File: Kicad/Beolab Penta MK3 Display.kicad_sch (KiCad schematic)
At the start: 6 parts, among them J1 Conn_01x07_Pin

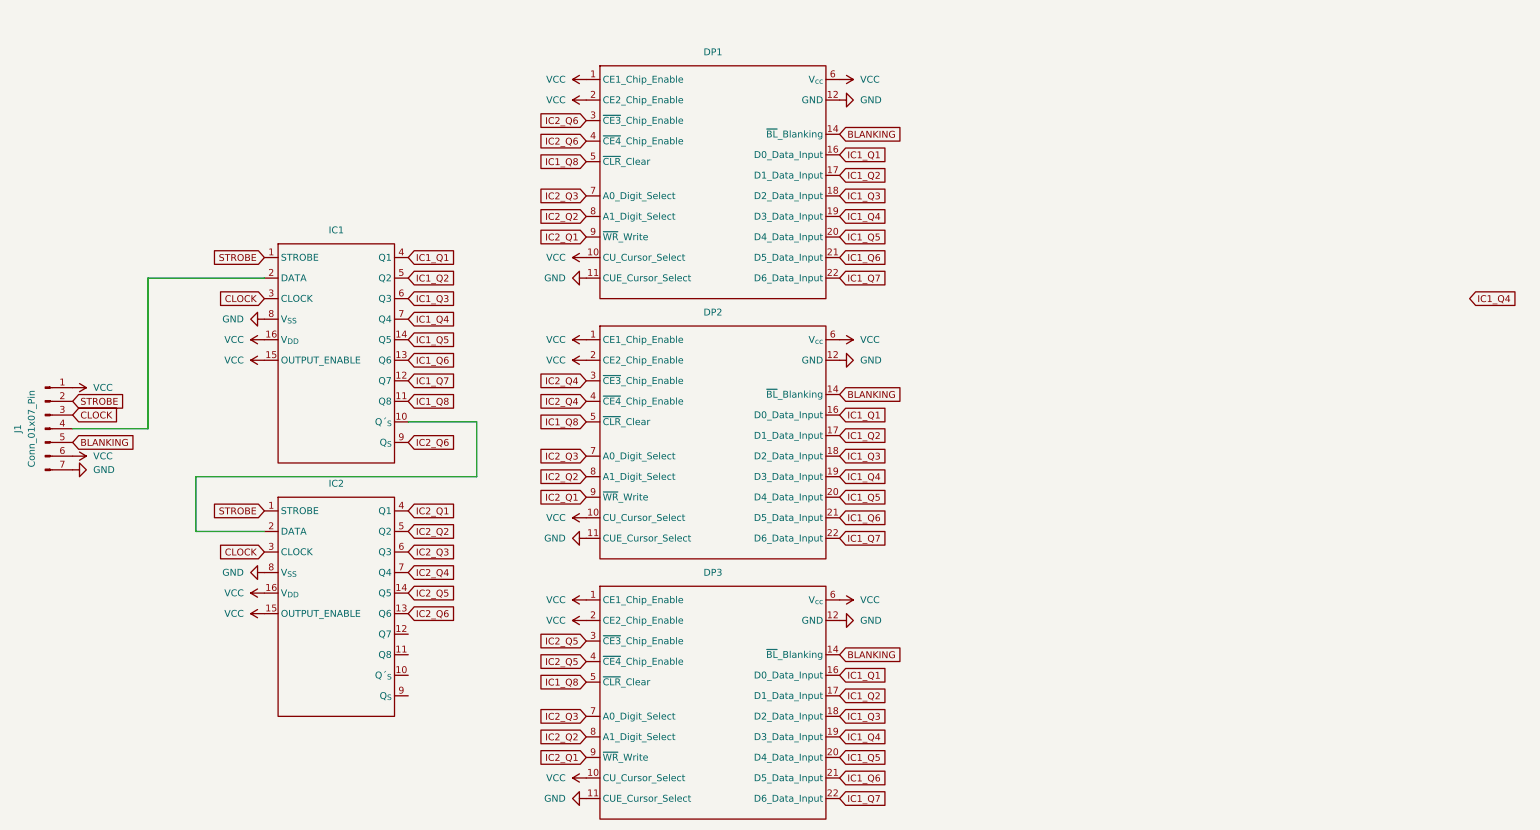
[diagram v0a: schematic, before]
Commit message: Update schematic to include arduino
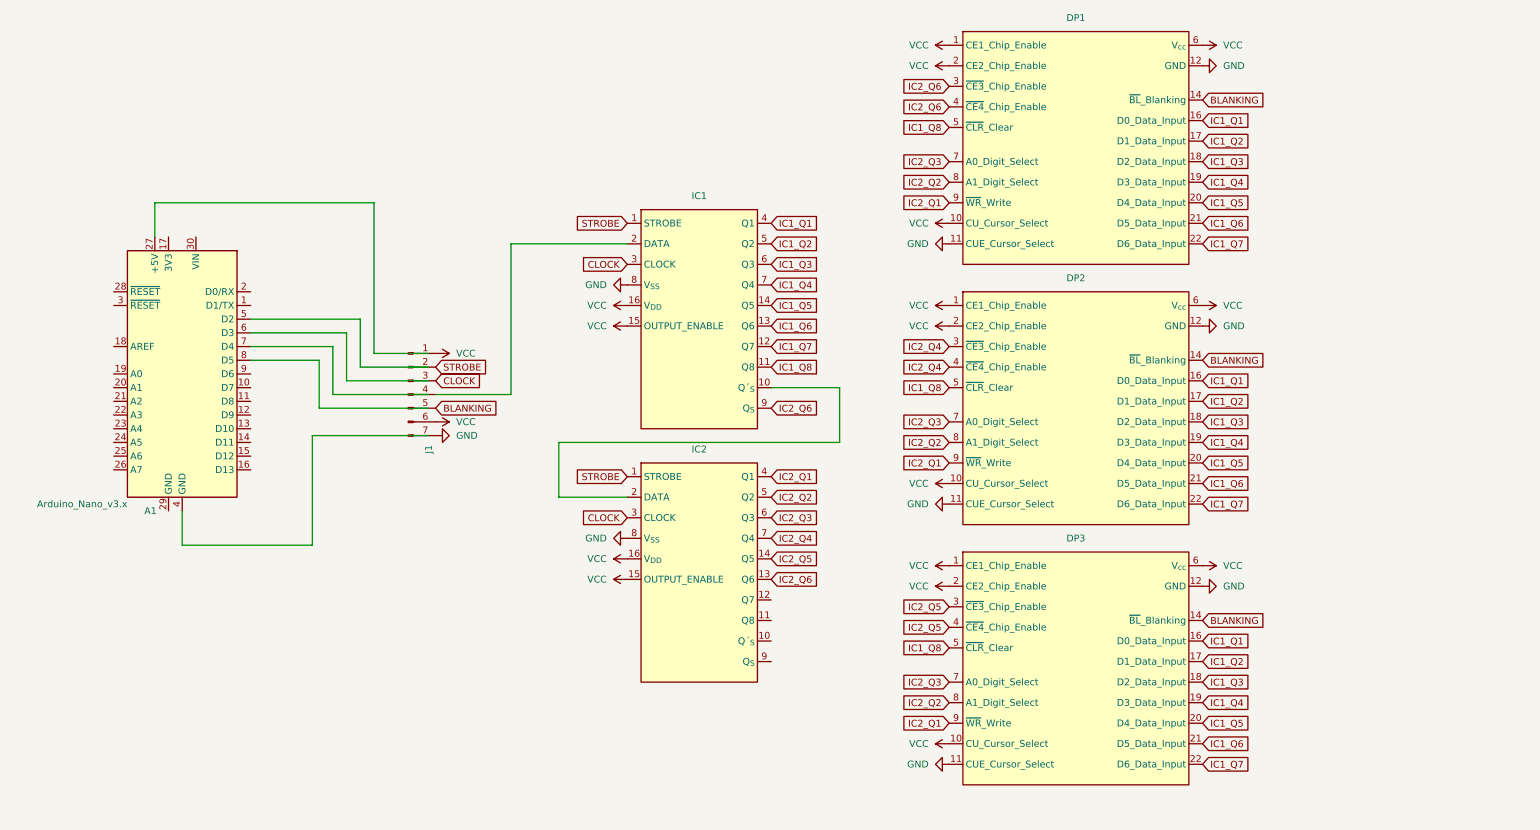
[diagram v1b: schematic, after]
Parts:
- added A1: Arduino_Nano_v3.x, Module:Arduino_Nano, symbol MCU_Module:Arduino_Nano_v3.x
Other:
- moved on the sheet: J1
